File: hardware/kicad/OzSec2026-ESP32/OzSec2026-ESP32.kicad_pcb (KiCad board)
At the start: 2 copper layers, 89.3 x 97.6 mm, 72 parts, among them J1 UART, J2 USB_C_Receptacle_USB2.0, J3 JTAG, J4 DISPLAY, J5 Conn_01x03_Socket, SW1 SW_Push, SW2 SW_Push, SW3 SW_Push, SW4 SW_Push, SW5 POWER, SW6 SW_Push, SW7 SW_Push, U1 USBLC6-2SC6, U2 ESP32-S3-WROOM-1, U3 ME4054BM5G-N, U4 TLV1117LV-33, U5 VSMY14940, X1 Simple_Addon_v2

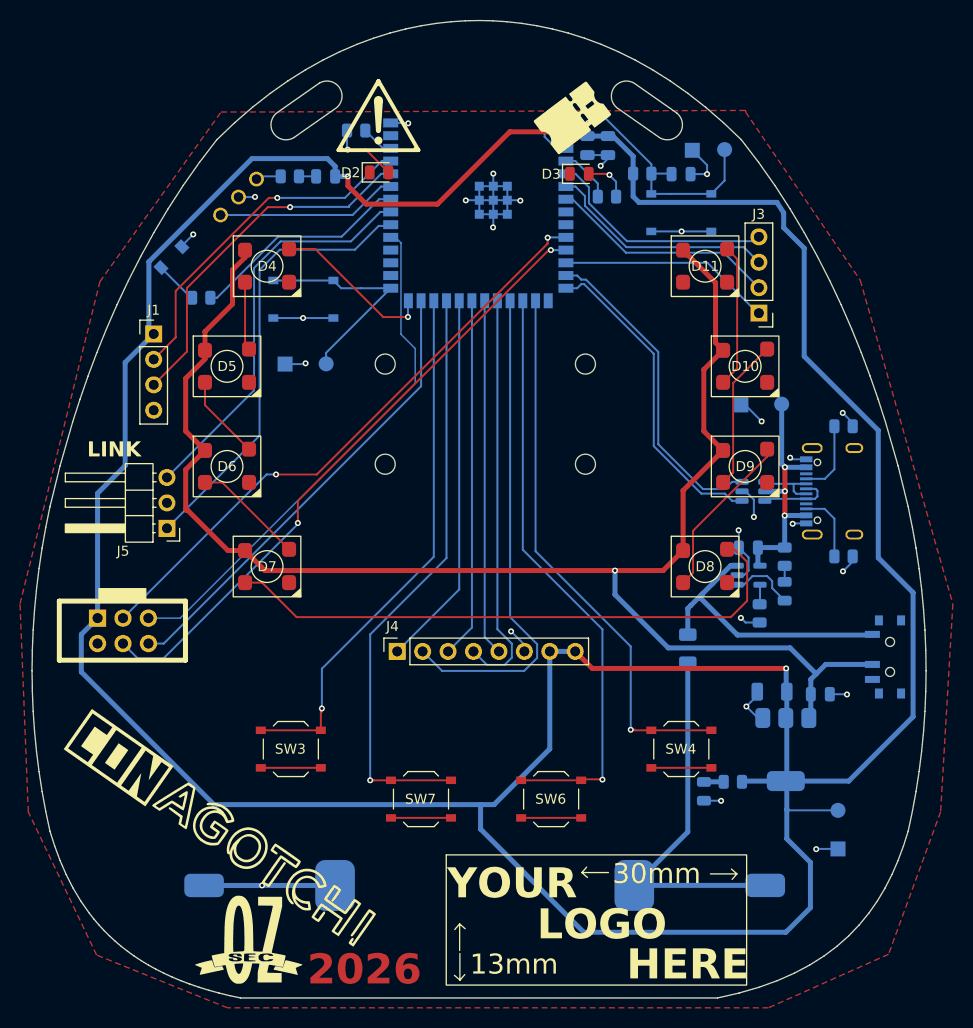
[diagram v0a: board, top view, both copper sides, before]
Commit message: Fabrication files for prototype 1.
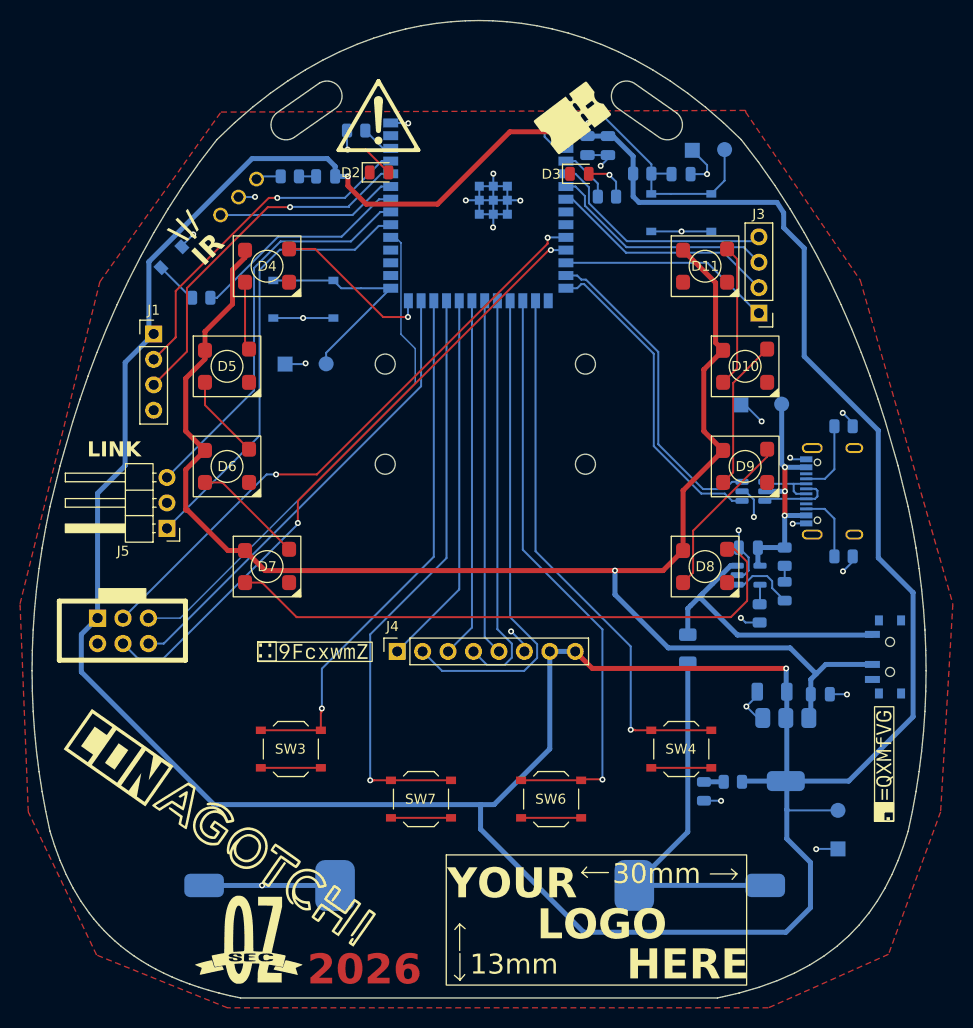
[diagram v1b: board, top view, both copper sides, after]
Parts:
- added REF**: Flag_Flip3, ozsec-2026:Flag_Flip3, B.Cu at (180.1, 80.1)
- added REF**: Flag_Flip2, ozsec-2026:Flag_Flip2, B.Cu at (166.5, 129.5)
- added REF**: Flag_Flip4, ozsec-2026:Flag_Flip4, F.Cu at (150.6, 102.0)
- added REF**: Flag_Flip1, ozsec-2026:Flag_Flip1, F.Cu at (207.1, 112.6)
- renumbered C7 to C5, C5 to C6, C6 to C7, R8 to R10, R11 to R4, R4 to R5, R9 to R6, R5 to R7, R6 to R8, R7 to R9, U5 to U2, U2 to U3, U3 to U4, U4 to U5
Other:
- board text added: "\|/ IR"

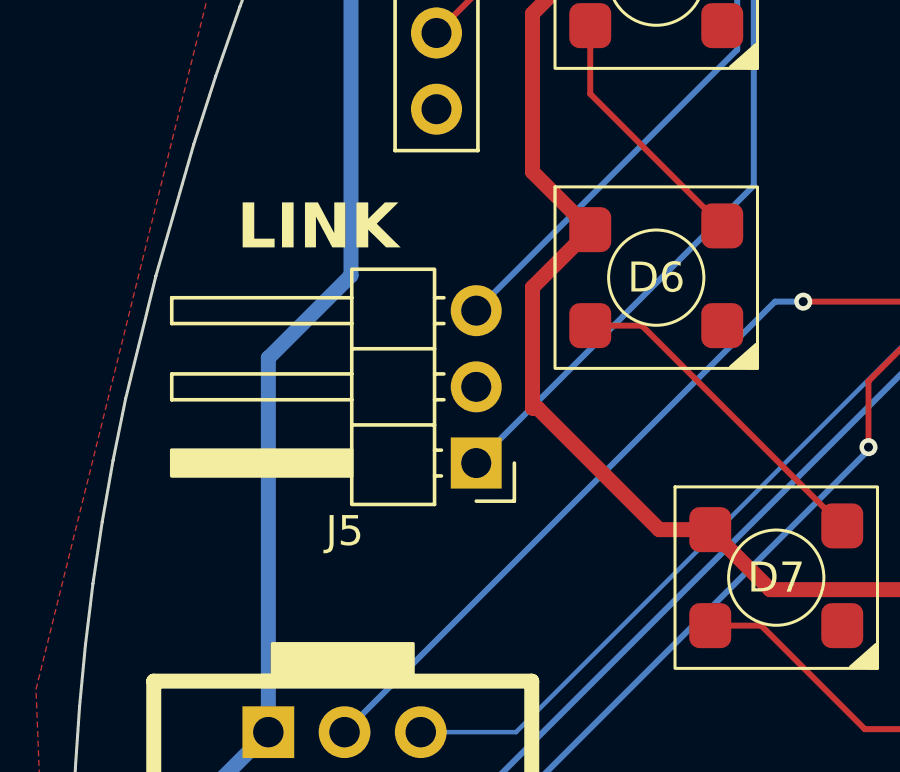
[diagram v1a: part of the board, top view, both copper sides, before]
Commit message: Added silkscreen to LINK connector.
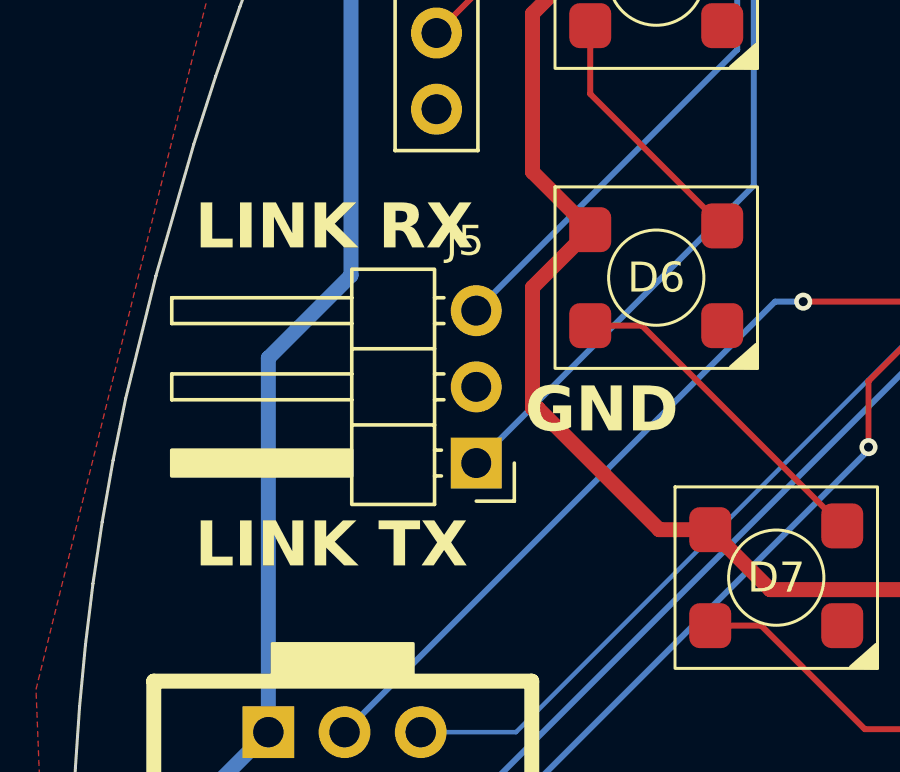
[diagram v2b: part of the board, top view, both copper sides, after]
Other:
- board text added: "LINK RX"
- board text added: "LINK TX"
- board text removed: "LINK"
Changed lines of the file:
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@@
 		(tags "Through hole angled pin header THT 1x03 2.54mm single row")
 		(property "Reference" "J5"
-			(at 4.385 -2.27 180)
+			(at 0.375 7.405 180)
 			(layer "F.SilkS")
 			(effects
@@
 		)
 	)
+	(gr_text "LINK TX"
+		(at 126 93 0)
+		(layer "F.SilkS")
+		(effects
+			(font
+				(size 1.5 1.5)
+				(thickness 0.3)
+				(bold yes)
+			)
+			(justify left bottom)
+		)
+	)
 	(gr_text " \\|/\n IR"
 		(at 138.525 64.15 45)
@@
 		)
 	)
-	(gr_text "LINK"
-		(at 127.4 82.4 0)
+	(gr_text "GND"
+		(at 137 88.5 0)
+		(layer "F.SilkS")
+		(effects
+			(font
+				(size 1.5 1.5)
+				(thickness 0.3)
+				(bold yes)
+			)
+			(justify left bottom)
+		)
+	)
+	(gr_text "LINK RX"
+		(at 126 82.4 0)
 		(layer "F.SilkS")
 		(effects

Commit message: Version 1.1 of PCB and some initial source files.
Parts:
- R10: value 2K -> 10K
- SW3, SW4, SW6, SW7: footprint ozsec-custom:SW_Push_1P1T_XKB_TS-1187A -> ozsec-custom:SW-SMD_4P-L4.5-W4.5-P3.00-LS6.8
- moved R2 3.34 mm to (205.7, 90.3), turned to -165 degrees
- moved J2 2.00 mm to (204.0, 84.0), turned to -75 degrees
- moved R3 1.62 mm to (202.3, 77.7), turned to 15 degrees
- renumbered U2 to D1, D9 to D10, D10 to D11, D11 to D12, D12 to D13, D1 to D2, D2 to D3, D3 to D4, D4 to D5, D5 to D6, D6 to D7, D7 to D8, D8 to D9, U3 to U2, LED1 to U3
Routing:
- net +3.3V: track 358.9 -> 355.4 mm
- net VBUS: track 25.3 -> 28.0 mm
- net /D-: track 38.5 -> 39.6 mm
- net GND: track 121.7 -> 120.6 mm
- net /D+: track 39.3 -> 40.4 mm
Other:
- board text added: "->"
- board text added: "<-"
- board text added: "CONAGOTCHI BADGE V1.1"
- board text added: "G|T|R|V"
- board text added: "M|I|O|K"
- board text added: "SELECT"
- board text added: "START"
- board text removed: "CONAGOTCHI BADGE V1.0"
